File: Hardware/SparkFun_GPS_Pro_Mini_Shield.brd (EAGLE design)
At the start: 20.3 x 40.6 mm, 23 parts, among them J1 USD_TINY, U1 EM406, U2 TXB0108, U3 AP2112K-3.3V

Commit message: Update file names and library
- Updated file names to follow standard
- Updated library with PROD_ID numbers
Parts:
- J1: value USD_TINY -> MICROSD_TINY; device uSD Socket temp:SLIM_USD -> GPS_Pro_Mini_temp:MICROSD_TINY
- U1: value EM406 -> GP735; device SparkFun-Connectors:EM406 -> GPS_Pro_Mini_temp:GP735
- turned U1 to 0 degrees
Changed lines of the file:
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@@
 <layer number="20" name="Dimension" color="15" fill="1" visible="yes" active="yes"/>
 <layer number="21" name="tPlace" color="16" fill="1" visible="yes" active="yes"/>
-<layer number="22" name="bPlace" color="14" fill="1" visible="no" active="yes"/>
+<layer number="22" name="bPlace" color="14" fill="1" visible="yes" active="yes"/>
 <layer number="23" name="tOrigins" color="15" fill="1" visible="yes" active="yes"/>
-<layer number="24" name="bOrigins" color="15" fill="1" visible="no" active="yes"/>
+<layer number="24" name="bOrigins" color="15" fill="1" visible="yes" active="yes"/>
 <layer number="25" name="tNames" color="7" fill="1" visible="no" active="yes"/>
 <layer number="26" name="bNames" color="7" fill="1" visible="no" active="yes"/>
@@
 <layer number="43" name="vRestrict" color="2" fill="10" visible="no" active="yes"/>
 <layer number="44" name="Drills" color="7" fill="1" visible="no" active="yes"/>
-<layer number="45" name="Holes" color="7" fill="1" visible="no" active="yes"/>
+<layer number="45" name="Holes" color="7" fill="1" visible="yes" active="yes"/>
 <layer number="46" name="Milling" color="3" fill="1" visible="no" active="yes"/>
 <layer number="47" name="Measures" color="7" fill="1" visible="no" active="yes"/>
@@
 </autorouter>
 <elements>
-<element name="J1" library="uSD Socket temp" package="SLIM_USD" value="USD_TINY" x="4.572" y="8.255"/>
+<element name="J1" library="GPS_Pro_Mini_temp" package="MICROSD_TINY" value="MICROSD_TINY" x="4.572" y="8.255">
+<attribute name="PROD_ID" value="CONN-13500" x="4.572" y="8.255" size="1.778" layer="27" display="off"/>
+</element>
 <element name="J2" library="SparkFun-Connectors" package="1X12_NO_SILK" value="" x="2.54" y="8.89" rot="R90"/>
 <element name="J3" library="SparkFun-Connectors" package="1X12_NO_SILK" value="" x="17.78" y="8.89" rot="R90"/>
@@
 <attribute name="PROD_ID" value="BATT-08044" x="10.033" y="5.461" size="1.778" layer="28" font="vector" ratio="15" rot="MR180" display="off"/>
 </element>
-<element name="U1" library="SparkFun-Connectors" package="EM406" value="EM406" x="12.7" y="34.925" rot="R180"/>
+<element name="U1" library="GPS_Pro_Mini_temp" package="GP735" value="GP735" x="12.7" y="34.925">
+<attribute name="PROD_ID" value="CONN-08249" x="12.7" y="34.925" size="1.778" layer="27" display="off"/>
+</element>
 <element name="J4" library="SparkFun-Connectors" package="1X06_NO_SILK" value="" x="16.51" y="39.37" rot="R180">
 <attribute name="PROD_ID" value="CONN-08437" x="16.51" y="39.37" size="1.778" layer="27" font="vector" ratio="15" rot="R180" display="off"/>

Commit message: Updated GPS label
Changed from GPS_PPS to GPS_CTRL
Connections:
- net GPS_PPS renamed GPS_CTRL
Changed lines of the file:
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@@
 <layer number="45" name="Holes" color="7" fill="1" visible="yes" active="yes"/>
 <layer number="46" name="Milling" color="3" fill="1" visible="no" active="yes"/>
-<layer number="47" name="Measures" color="7" fill="1" visible="no" active="yes"/>
+<layer number="47" name="Measures" color="7" fill="1" visible="yes" active="yes"/>
 <layer number="48" name="Document" color="7" fill="1" visible="no" active="yes"/>
 <layer number="49" name="Reference" color="7" fill="1" visible="no" active="yes"/>
@@
 <wire x1="7.366" y1="26.67" x2="8.7" y2="26.67" width="0.508" layer="16"/>
 </signal>
-<signal name="GPS_PPS">
+<signal name="GPS_CTRL">
 <contactref element="U1" pad="6"/>
 <contactref element="J4" pad="6"/>

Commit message: Added board designer name and version number
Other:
- board text added: "v01"
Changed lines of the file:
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@@
 <layer number="45" name="Holes" color="7" fill="1" visible="yes" active="yes"/>
 <layer number="46" name="Milling" color="3" fill="1" visible="no" active="yes"/>
-<layer number="47" name="Measures" color="7" fill="1" visible="yes" active="yes"/>
+<layer number="47" name="Measures" color="7" fill="1" visible="no" active="yes"/>
 <layer number="48" name="Document" color="7" fill="1" visible="no" active="yes"/>
 <layer number="49" name="Reference" color="7" fill="1" visible="no" active="yes"/>
@@
 <text x="13.97" y="38.1" size="0.8128" layer="22" font="vector" ratio="15" rot="MR180" align="bottom-center">3.3V</text>
 <text x="16.129" y="38.1" size="0.8128" layer="22" font="vector" ratio="15" rot="MR270" align="center-left">GND</text>
+<text x="5.207" y="0.254" size="1.27" layer="16" font="vector" ratio="15" rot="MR0">v01</text>
 </plain>
 <attributes>

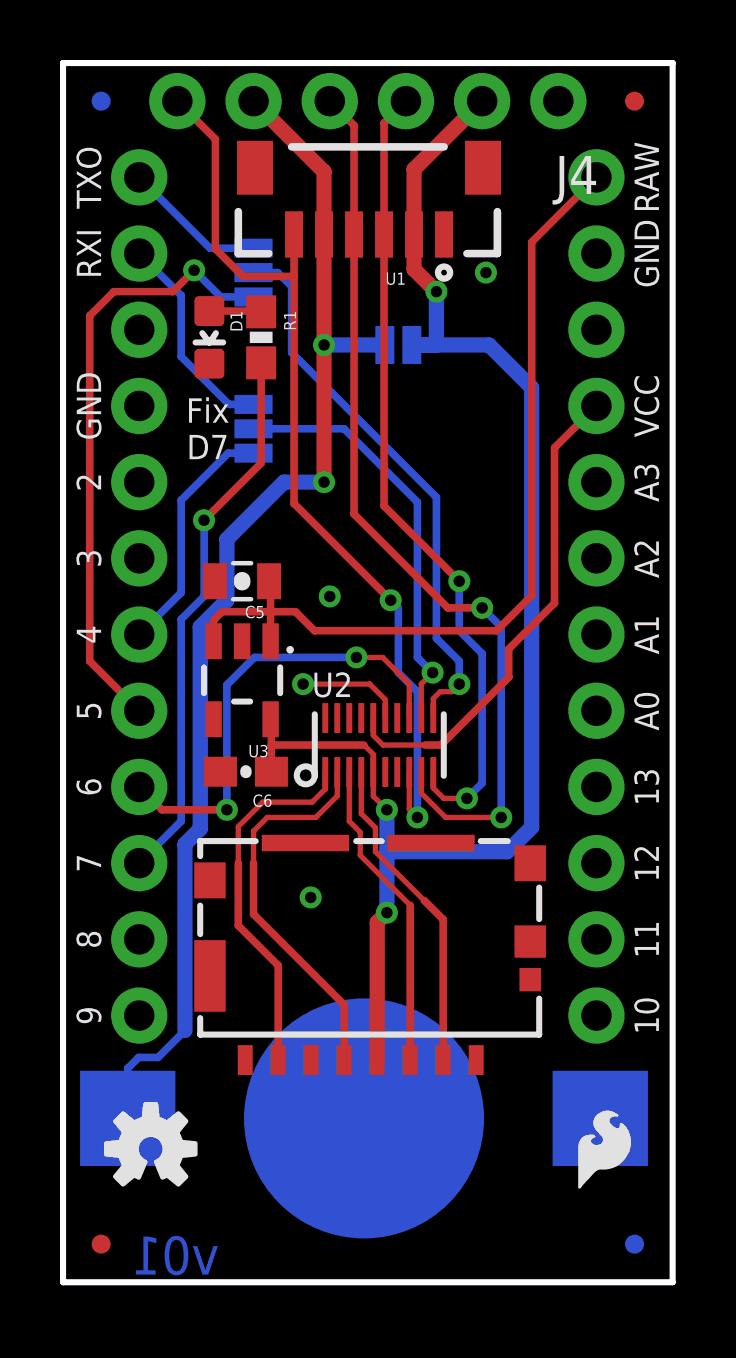
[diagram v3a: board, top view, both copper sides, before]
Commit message: Design Review Changes
- Fixed SPI traces
- Moved VIN of regulator to VIN instead of RAW
- Removed jumpers for software/hardware uart with DPDT switch
- Added product name to board
- Replaced coin cell battery with two PTH pins to make the board smaller
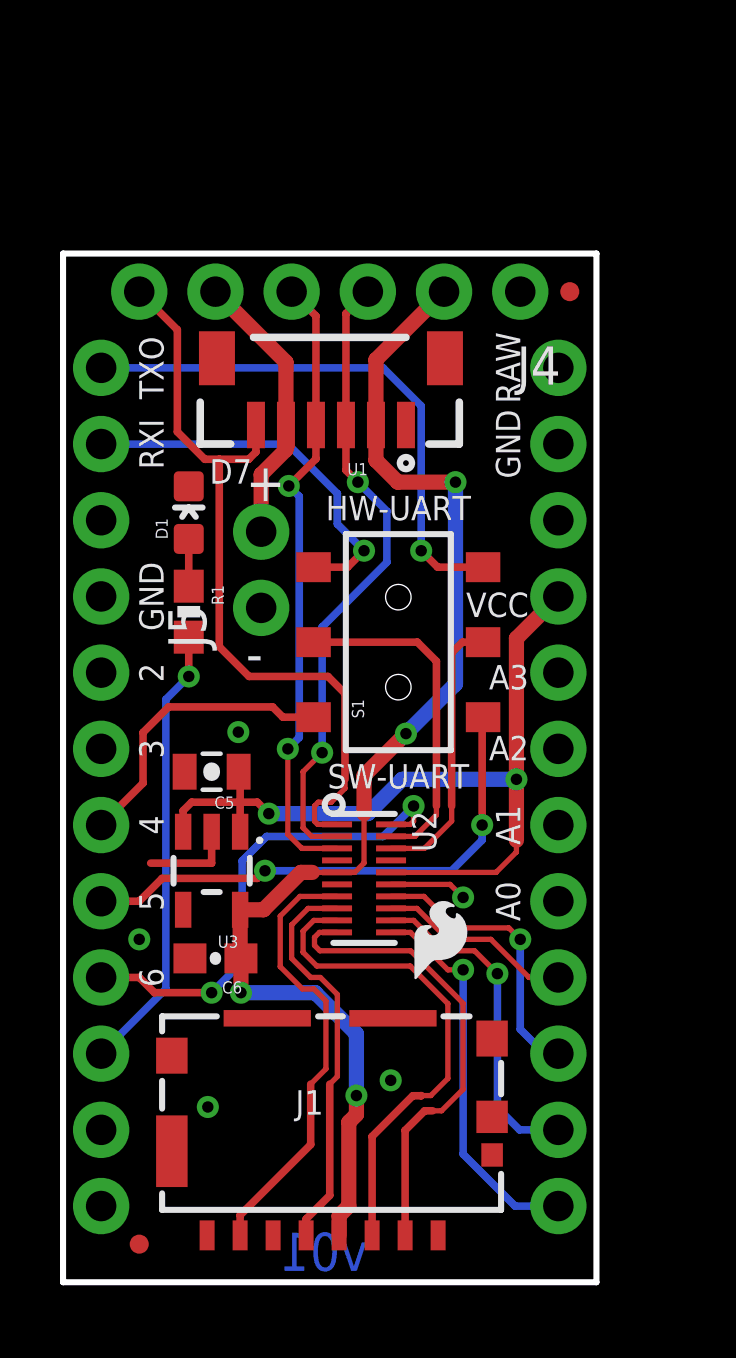
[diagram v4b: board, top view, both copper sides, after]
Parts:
- removed BAT1: 12MM Coin Cell, SparkFun-Electromechanical:BATTCON_12MM
- removed FD3, FD4: FIDUCIALUFIDUCIAL, SparkFun-Aesthetics:MICRO-FIDUCIAL
- removed JP1: (no value), SparkFun-Passives:PAD-JUMPER-2-NO_YES_SILK
- removed JP2, JP3: (no value), SparkFun-Passives:PAD-JUMPER-3-2OF3_NC_BY_PASTE_YES_SILK_FULL_BOX
- added J5: (no value), SparkFun-Connectors:1X02_NO_SILK
- added S1: DPDT, SparkFun-Electromechanical:AYZ0202
- moved R1 9.46 mm to (4.19, 22.4)
- moved LOGO3 8.87 mm to (11.4, 9.78)
- moved FD2 6.71 mm to (16.9, 33.0)
- moved J2 6.48 mm to (1.27, 2.54)
- moved J3 6.48 mm to (16.5, 2.54)
- moved U1 6.48 mm to (11.4, 28.6)
- moved J4 6.48 mm to (15.2, 33.0)
- moved U3 6.43 mm to (4.95, 13.7)
- moved C5 6.43 mm to (4.95, 17.0)
- moved C6 6.31 mm to (5.08, 10.8)
- moved J1 5.98 mm to (3.30, 2.41)
- moved D1 5.88 mm to (4.19, 25.7), turned to 0 degrees
- moved LOGO4 5.71 mm to (6.60, 17.8)
- moved U2 4.47 mm to (10.0, 13.5), turned to 270 degrees
- moved LOGO1 2.81 mm to (5.59, 3.56), flipped to the bottom
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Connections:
- removed net HV_CS: U2.17
- removed net HV_MISO: U2.20
- removed net HV_MOSI: U2.18
- removed net HV_SCK: U2.19
- net 0/RX: now also S1.3; no longer JP2.3
- net 1/TX: now also S1.6; no longer JP3.3
- net 10: now also U2.11
- net 11: now also U2.12
- net 12: now also U2.14
- net 13: now also U2.13
- net 3.3V: no longer JP1.2
- net 4: now also S1.1; no longer JP2.1
- net 5: now also S1.4; no longer JP3.1
- net 6: now also U2.20; no longer U2.13
- net GND: now also J5.1; no longer BAT1.GND
- net GPS_CTRL: now also U2.1; no longer U2.8
- net GPS_RX: now also J4.4, U1.4, U2.3; no longer J4.3, U1.3, U2.10
- net GPS_TX: now also J4.3, U1.3, U2.2; no longer J4.4, U1.4, U2.9
- net RX: now also S1.2, U2.19; no longer JP2.2, U2.12
- net SD_CS: now also U2.10; no longer U2.4
- net SD_DI: now also U2.9; no longer U2.3
- net SD_DO: now also U2.7; no longer U2.1
- net SD_SCK: now also U2.8; no longer U2.2
- net TX: now also S1.5, U2.18; no longer JP3.2, U2.11
- net VCC: now also C5.1, U3.1, U3.3
- net VIN: no longer C5.1, U3.1, U3.3
- net V_BATT: now also J5.2; no longer BAT1.PWR@1, JP1.1
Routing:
- net V_BATT: track 40.8 -> 9.32 mm, vias 2 -> 0
- net VIN: track 29.1 -> 0.00 mm
- net 1/TX: track 4.79 -> 18.3 mm, vias 0 -> 1
- net 10: track 0.00 -> 13.0 mm, vias 0 -> 1
- net VCC: track 16.4 -> 28.2 mm, vias 0 -> 2
- net 11: track 0.00 -> 11.1 mm, vias 0 -> 1
- net TX: track 18.7 -> 9.20 mm, vias 1 -> 0
- net 12: track 0.00 -> 9.50 mm, vias 0 -> 1
- net GPS_TX: track 30.6 -> 21.1 mm
- net 3.3V: track 50.4 -> 42.4 mm, vias 3 -> 4
- net 13: track 0.00 -> 6.53 mm
- net SD_DI: track 10.4 -> 16.6 mm
- net GPS_RX: track 26.9 -> 20.9 mm
- net 0/RX: track 7.09 -> 12.7 mm, vias 0 -> 1
- net GPS_CTRL: track 31.2 -> 26.0 mm, vias 2 -> 0
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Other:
- board size 20.3 x 40.6 mm -> 17.8 x 34.3 mm
- board text added: "+"
- board text added: "-"
- board text added: "CTR"
- board text added: "D7"
- board text added: "HW-UART"
- board text added: "Pro Mini GPS Shield"
- board text added: "SW-UART"
- board text removed: "0"
- board text removed: "1"
- board text removed: "CTRL"
- board text removed: "Fix D7"

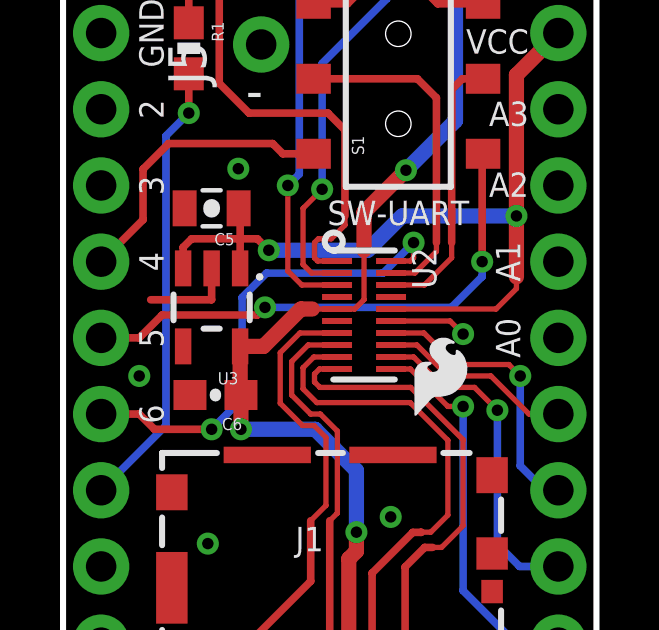
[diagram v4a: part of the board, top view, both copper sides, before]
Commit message: QC Changes
- shorted output enable to VCCA
- added note of PCB thickness to tDocu
- added VBATT to bottom silk for 2-pin vbatt header
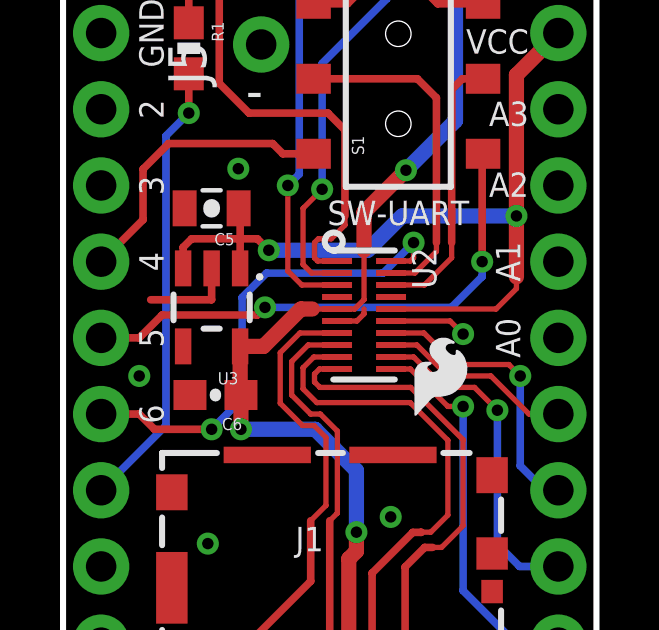
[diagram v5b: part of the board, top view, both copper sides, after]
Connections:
- net 3.3V: now also U2.6
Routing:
- net 3.3V: track 42.4 -> 43.6 mm
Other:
- board text added: "PCB thickness = 0.032""
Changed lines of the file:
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@@
 <layer number="20" name="Dimension" color="15" fill="1" visible="yes" active="yes"/>
 <layer number="21" name="tPlace" color="16" fill="1" visible="yes" active="yes"/>
-<layer number="22" name="bPlace" color="14" fill="1" visible="yes" active="yes"/>
+<layer number="22" name="bPlace" color="14" fill="1" visible="no" active="yes"/>
 <layer number="23" name="tOrigins" color="15" fill="1" visible="yes" active="yes"/>
-<layer number="24" name="bOrigins" color="15" fill="1" visible="yes" active="yes"/>
+<layer number="24" name="bOrigins" color="15" fill="1" visible="no" active="yes"/>
 <layer number="25" name="tNames" color="7" fill="1" visible="no" active="yes"/>
 <layer number="26" name="bNames" color="7" fill="1" visible="no" active="yes"/>
@@
 <layer number="43" name="vRestrict" color="2" fill="10" visible="no" active="yes"/>
 <layer number="44" name="Drills" color="7" fill="1" visible="no" active="yes"/>
-<layer number="45" name="Holes" color="7" fill="1" visible="yes" active="yes"/>
+<layer number="45" name="Holes" color="7" fill="1" visible="no" active="yes"/>
 <layer number="46" name="Milling" color="3" fill="1" visible="no" active="yes"/>
-<layer number="47" name="Measures" color="7" fill="1" visible="no" active="yes"/>
+<layer number="47" name="Measures" color="7" fill="1" visible="yes" active="yes"/>
 <layer number="48" name="Document" color="7" fill="1" visible="no" active="yes"/>
 <layer number="49" name="Reference" color="7" fill="1" visible="no" active="yes"/>
@@
 <text x="2.54" y="30.48" size="0.8128" layer="22" font="vector" ratio="15" rot="MR90" align="bottom-center">TXO</text>
 <text x="2.54" y="27.94" size="0.8128" layer="22" font="vector" ratio="15" rot="MR90" align="bottom-center">RXI</text>
+<text x="22.86" y="13.97" size="1.27" layer="51" font="vector" ratio="15">PCB thickness = 0.032"</text>
 </plain>
 <attributes>
@@
 <wire x1="8.4052875" y1="9.652" x2="9.779" y2="8.2782875" width="0.508" layer="16"/>
 <wire x1="9.779" y1="8.2782875" x2="9.779" y2="6.223" width="0.508" layer="16"/>
+<contactref element="U2" pad="6"/>
+<wire x1="9.133" y1="13.262" x2="9.7960875" y2="13.262" width="0.1778" layer="1"/>
+<wire x1="9.7960875" y1="13.262" x2="10.033" y2="13.4989125" width="0.1778" layer="1"/>
+<wire x1="10.033" y1="13.4989125" x2="10.033" y2="13.662" width="0.1778" layer="1"/>
 </signal>
 <signal name="GND">
